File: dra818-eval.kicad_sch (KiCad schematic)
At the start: 0 parts

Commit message: Initial schematic
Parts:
- added AE1: Antenna, symbol Device:Antenna_Shield
- added C1, C3: 100nF, symbol Device:C
- added C2: 1uF, symbol Device:C
- added J1: FTDI Serial, symbol Connector_Generic:Conn_01x06
- added J2: TRRS Headset, symbol Connector_Audio:AudioJack4
- added R1, R2: 10k, symbol Device:R_US
- added R3: 150k, symbol Device:R_US
- added RV1: 10k, symbol Device:R_Potentiometer_US
- added SW1: TX_PWR, symbol Switch:SW_SPST
- added SW2: PTT, symbol Switch:SW_Push
- added U1: DRA818V, DORJI_DRA818V, symbol DRA818V:DRA818V
- added U2: LM4871M, LM4871M:SOIC127P599X175-8N, symbol LM4871M:LM4871M
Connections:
- new net: C1.2, RV1.1
- new net: C2.1, U2.2 (BYPASS), U2.3 (+IN)
- new net: R3.1, RV1.2, U2.4 (-IN)
- new net +3V3: C3.1, J1.3 (Pin_3), R1.1, R2.1, U1.6 (PD), U1.8 (VBAT), U2.6 (VDD)
- new net AF_OUT: C1.1, U1.3 (AF_OUT)
- new net ANT: AE1.1 (A), U1.12 (ANT)
- new net AUD_GND: J2.R2, U2.8 (V02)
- new net AUD_L: J2.R1, J2.T, R3.2, U2.5 (V01)
- new net CTS: J1.2 (Pin_2)
- new net DTR: J1.6 (Pin_6)
- new net GND: AE1.2 (Shield), C2.2, C3.2, J1.1 (Pin_1), RV1.3, SW1.1 (A), SW2.1, U1.10 (GND), U1.9 (GND), U2.7 (GND)
- new net H/L: SW1.2 (B), U1.7 (H/L)
- new net MIC: J2.S, U1.18 (MIC_IN)
- new net PTT: R1.2, SW2.2, U1.5 (PTT)
- new net RXI: J1.5 (Pin_5), U1.17 (TXD)
- new net SQ: R2.2, U1.1 (SQ), U2.1 (SHUTDOWN)
- new net TXO: J1.4 (Pin_4), U1.16 (RXD)
- no-connect marks 0 -> 1
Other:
- note added: "Leave floating for high power"
- note added: "Logic 0 for TX"
- note added: "Logic 0 for low power"
- note added: "Logic 1 for RX"
- note added: "TODO: Low pass filter"

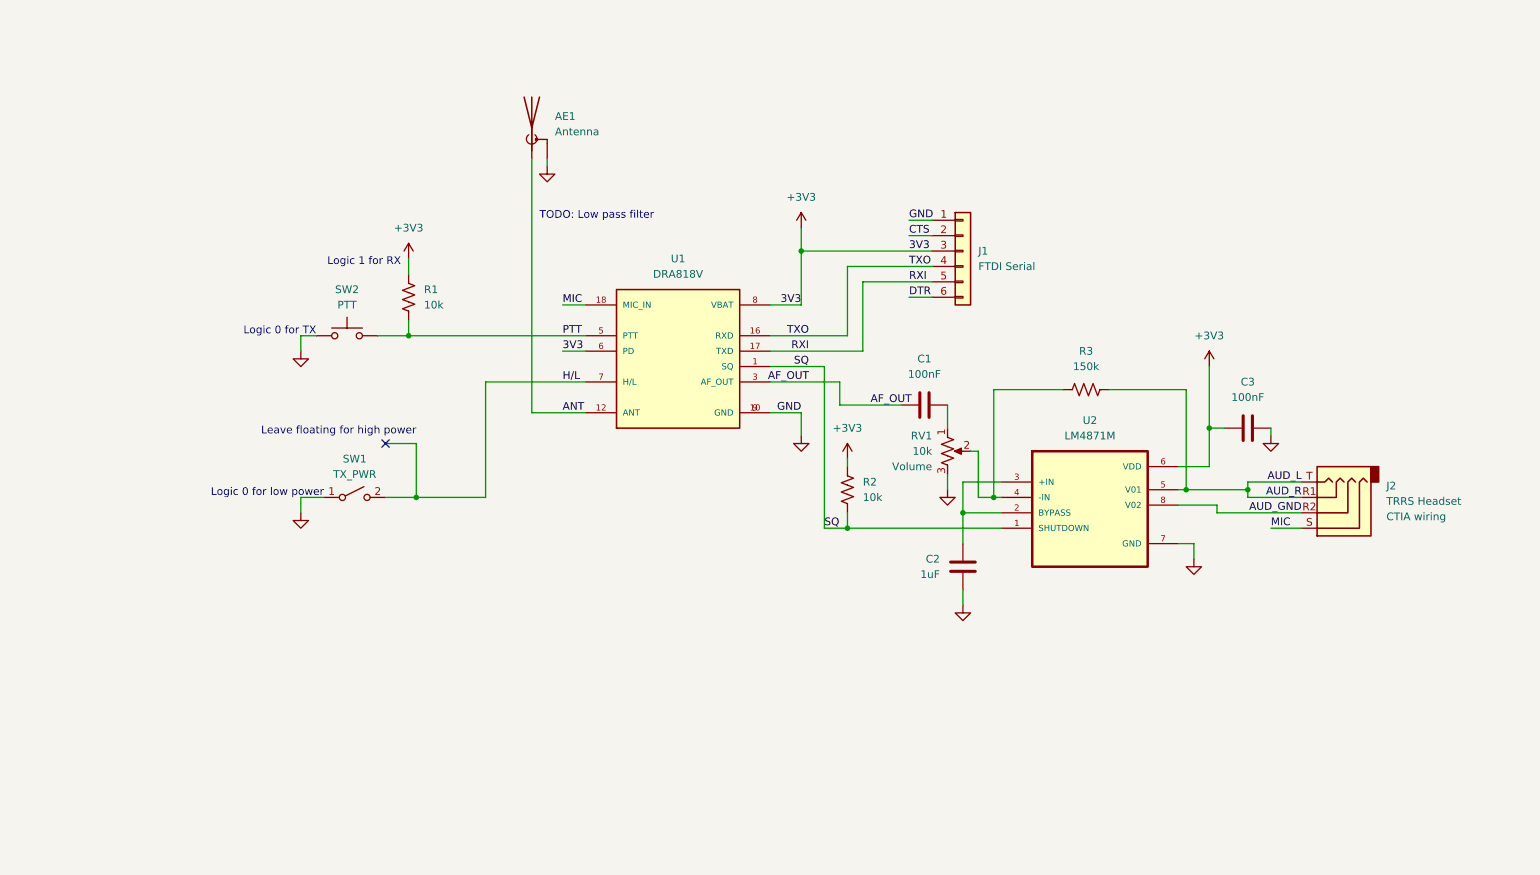
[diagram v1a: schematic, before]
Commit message: Electrical rules check
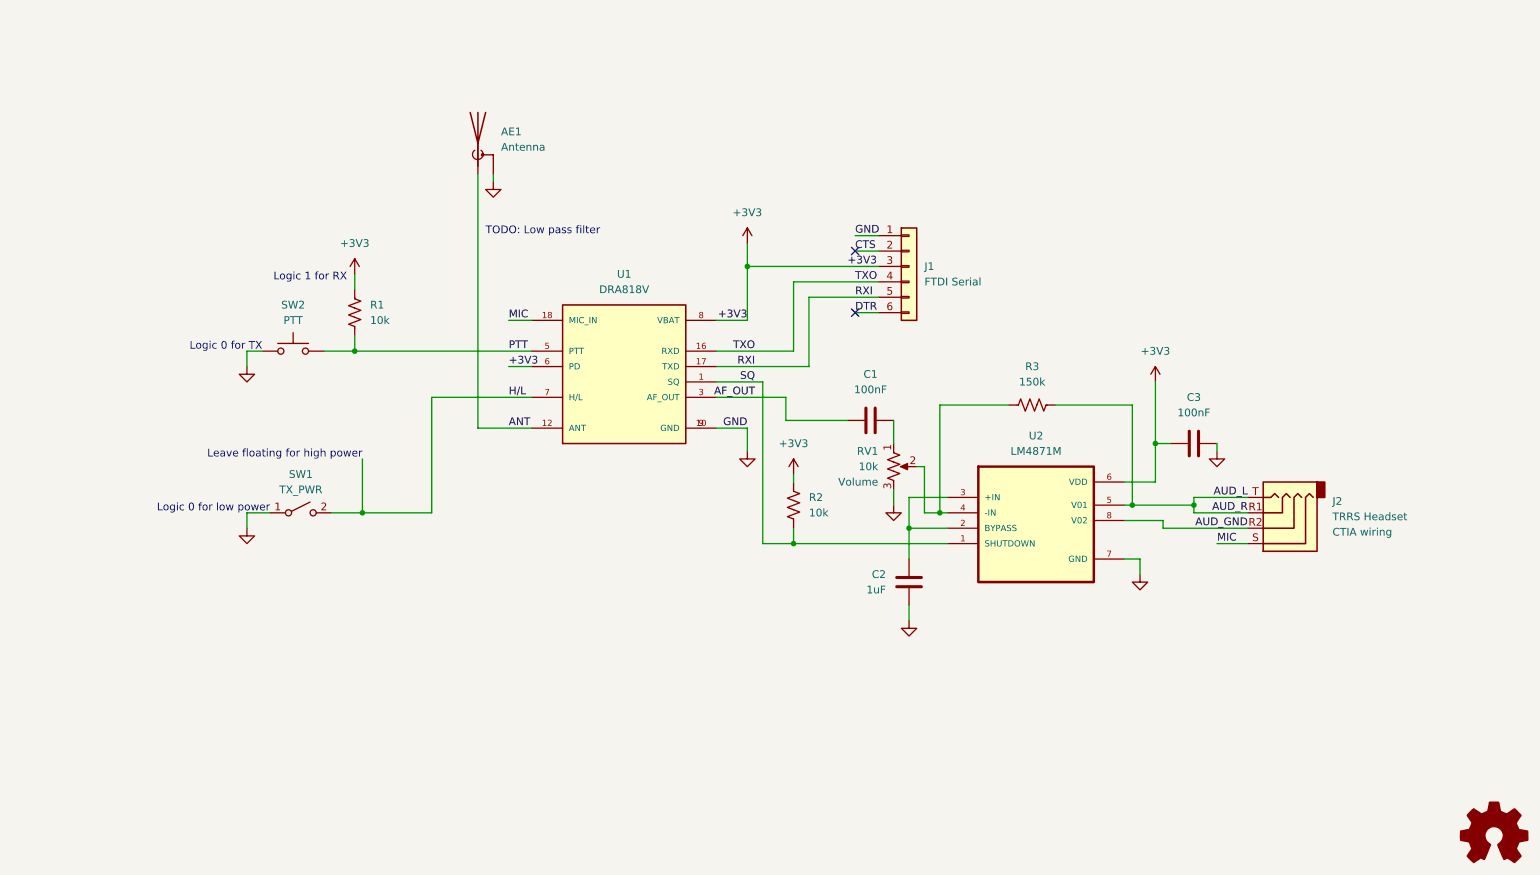
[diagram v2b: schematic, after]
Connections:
- no-connect marks 1 -> 2
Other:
- company: (none) -> C Keller K0SWE
- title: (none) -> DRA818 Evaluation
- moved on the sheet: AE1, C1, C2, C3, J1, J2, R1, R2, R3, RV1, SW1, SW2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

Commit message: Add LPF and LEDs
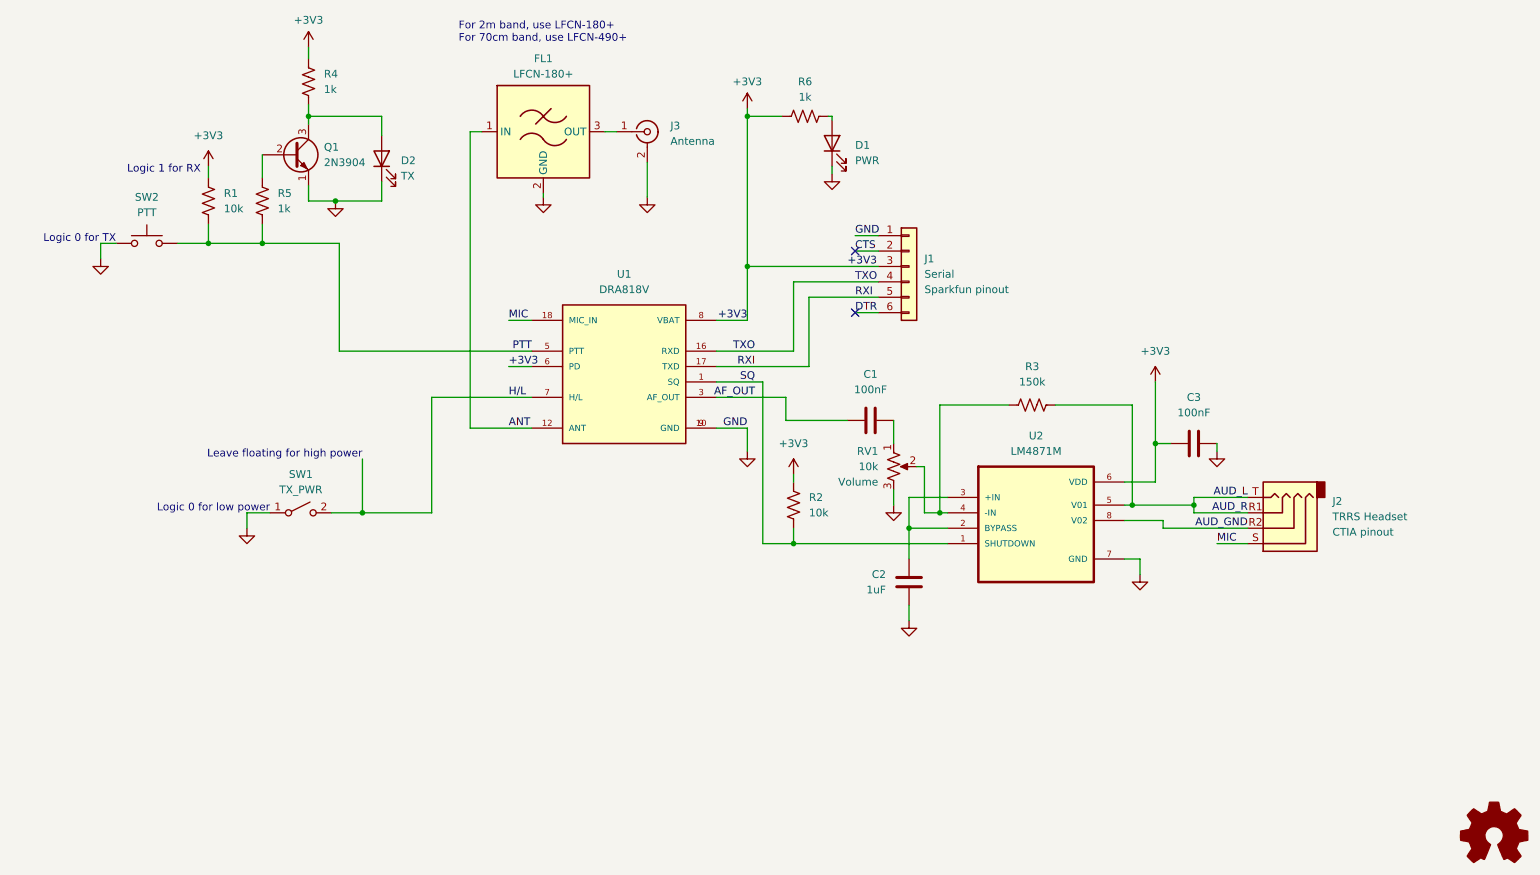
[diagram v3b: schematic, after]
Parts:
- removed AE1: Antenna, symbol Device:Antenna_Shield
- added D1: PWR, symbol Device:LED
- added D2: TX, symbol Device:LED
- added FL1: LFCN-180+, Filter:Filter_Mini-Circuits_FV1206, symbol RF_Filter:LFCN-180
- added J3: Antenna, symbol Connector:Conn_Coaxial
- added Q1: 2N3904, Package_TO_SOT_THT:TO-92_Inline, symbol Transistor_BJT:2N3904
- added R4, R5, R6: 1k, symbol Device:R_US
- J1: value FTDI Serial -> Serial; footprint (none) -> Connector_PinHeader_2.54mm:PinHeader_1x06_P2.54mm_Horizontal
- U1: footprint DORJI_DRA818V -> DRA818:DORJI_DRA818V
- U2: footprint LM4871M:SOIC127P599X175-8N -> LM4871:SOIC127P599X175-8N
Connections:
- net +3V3: now also R4.1, R6.1
- net ANT: now also FL1.1 (IN)
- net GND: now also D1.1 (K), D2.1 (K), FL1.2 (GND), FL1.4 (GND), J3.2 (Ext), Q1.1 (E)
- net PTT: now also R5.2
- new net: D1.2 (A), R6.2
- new net: D2.2 (A), Q1.3 (C), R4.2
- new net: Q1.2 (B), R5.1
- new net: FL1.3 (OUT), J3.1 (In)
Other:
- note added: "For 2m band, use LFCN-180+ For 70cm band, use LFCN-490+"
- note removed: "TODO: Low pass filter"
- moved on the sheet: R1, SW2
